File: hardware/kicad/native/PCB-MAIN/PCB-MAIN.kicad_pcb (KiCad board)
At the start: 6 copper layers, 110 x 75 mm, 251 parts, among them J10 U.FL-R-SMT-1(60), J11 USB4105-GF-A-120, J12 MEM2052-00-195-00-A, J13 504050-0291, J6 2336582-1, J7 2336582-1, J8 U.FL-R-SMT-1(60), J9 U.FL-R-SMT-1(60), Q1 MMBT3904,215, Q2 MMBT3904,215, Q3 MMBT3904,215, Q4 Si1016X-T1-GE3, U1 STM32U585VIT6Q, U10 E22-900M22S, U11 MDBT50Q-P1MV2, U13 TS3A27518EPWR, U14 ESDALC6V1-5P6, U15 ESDALC6V1-5P6, U16 SN74AXC8T245PWR, U17 SN74LVC32APWR, U18 SN74AXC1T45DRLR, U19 TPD4E05U06DQAR, U2 W25Q512JVFIQ, U20 TPD4E05U06DQAR, U21 TPD4E05U06DQAR, U22 TPD4E05U06DQAR, U23 TPD4E05U06DQAR, U24 TPD4E05U06DQAR, U25 TPD2EUSB30DRTR, U26 TPD2EUSB30DRTR, U27 TPD4E05U06DQAR, U3 LIS2DW12TR, U4 STTS22HTR, U5 LT6000IDCB#TRMPBF, U6 SN74LVC1G07DBVR, U7 SN74AXC8T245PWR, U8 BG95-M3, U9 MAX-M10S-00B, X1 SiT1552AI-JE-DCC-32.768D

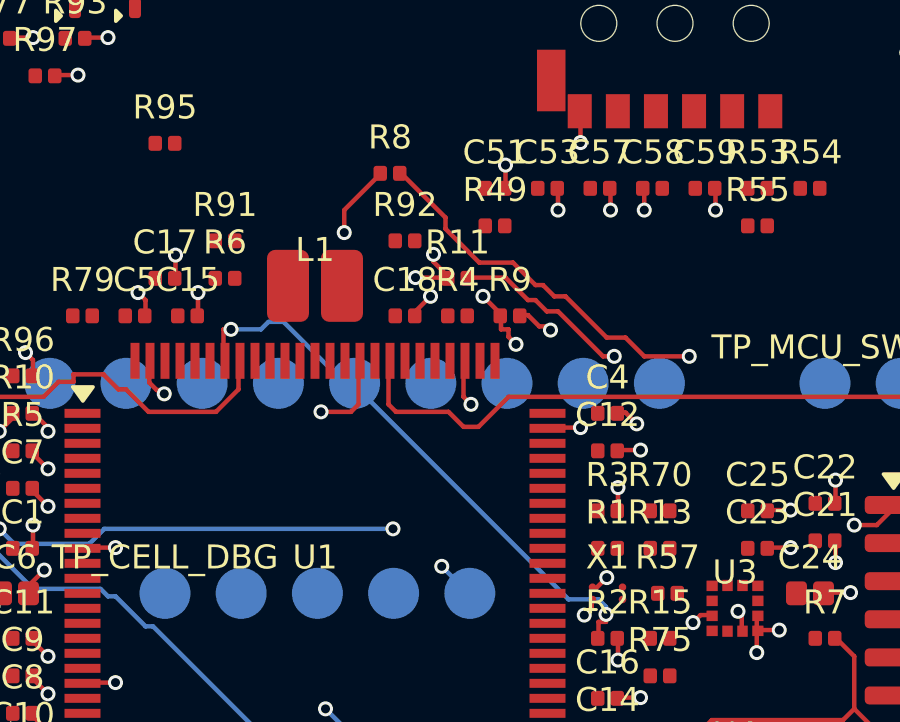
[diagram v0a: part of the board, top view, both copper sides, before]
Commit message: Apply accepted USB termination placement ECO
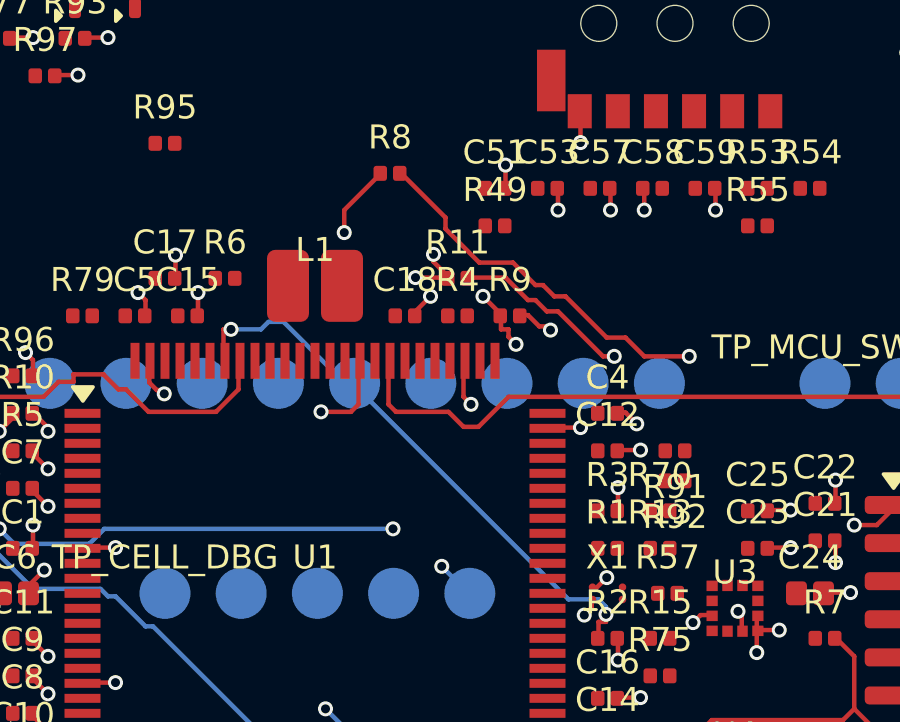
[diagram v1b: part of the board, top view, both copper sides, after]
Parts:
- moved R91 16.6 mm to (64.0, 25.2), turned to 0 degrees
- moved R92 12.0 mm to (64.0, 26.2), turned to 0 degrees
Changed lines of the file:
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@@
   )
   (footprint "" (layer "F.Cu")
-    (at 55 18.25 180)
+    (at 64 26.25)
     (property "DIONEA_COURTYARD_SOURCE" "PCB_MAIN_PASSIVE_COURTYARD_RULE_REV_A")
     (property "DIONEA_COURTYARD_STATUS" "CONTROLLED_PAD_ENVELOPE_PLUS_0.25_MM")
@@
   )
   (footprint "" (layer "F.Cu")
-    (at 49 18.25 180)
-    (property "DIONEA_COURTYARD_SOURCE" "PCB_MAIN_PASSIVE_COURTYARD_RULE_REV_A")
-    (property "DIONEA_COURTYARD_STATUS" "CONTROLLED_PAD_ENVELOPE_PLUS_0.25_MM")
+    (at 64 25.25)
+    (property "DIONEA_COURTYARD_SOURCE" "PCB_MAIN_PASSIVE_COURTYARD_RULE_REV_A")
+    (property "DIONEA_COURTYARD_STATUS" "CONTROLLED_PAD_ENVELOPE_PLUS_0.25_MM")

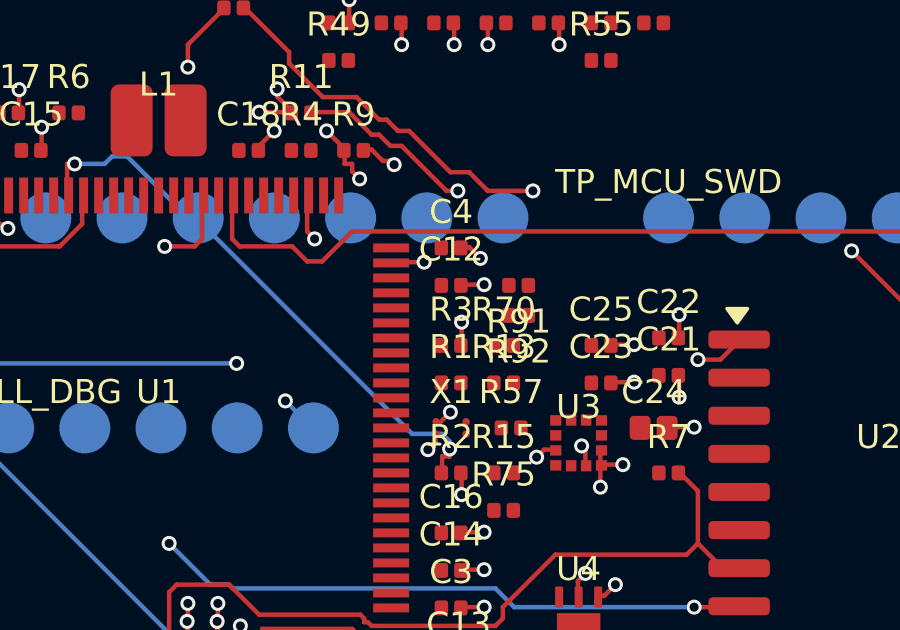
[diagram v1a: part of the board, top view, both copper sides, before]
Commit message: Apply accepted USB MCU source routing
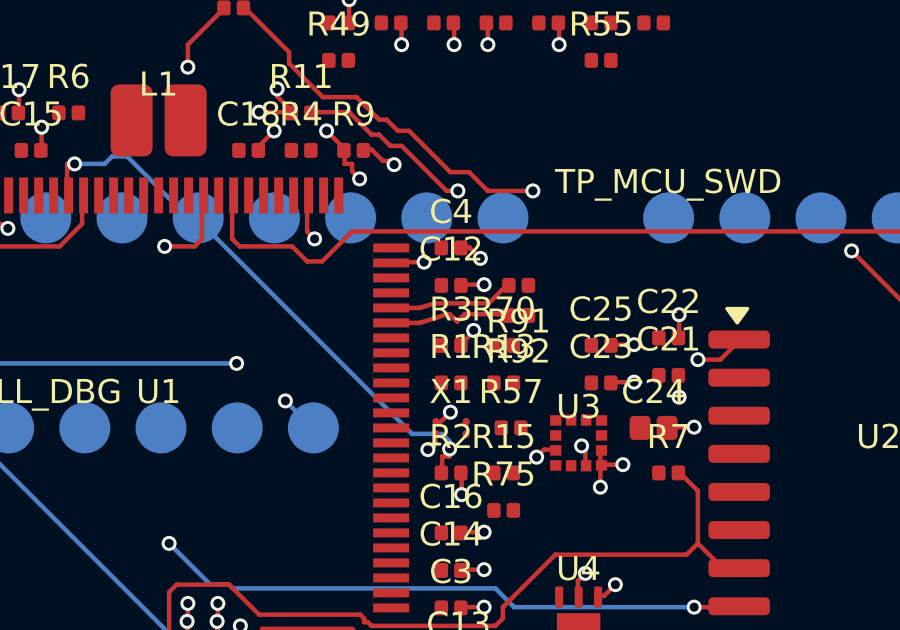
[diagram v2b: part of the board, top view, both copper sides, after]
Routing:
- net USB_DM_U1: track 0.00 -> 4.18 mm
- net USB_DP_U1: track 0.00 -> 4.18 mm
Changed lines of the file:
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@@
   (segment (start 64.849999 30.725) (end 64.599999 30.975) (width 0.15) (layer "F.Cu") (net 45))
   (segment (start 81.475 20.475) (end 81.475 20.1) (width 0.15) (layer "F.Cu") (net 45))
-  (segment (start 62.1 27.225) (end 62.1 26.475) (width 0.15) (layer "F.Cu") (net 45))
+  (segment (start 62.1 27.225) (end 62.5 26.75) (width 0.15) (layer "F.Cu") (net 45))
   (segment (start 65.974999 35.1) (end 66.224999 34.85) (width 0.15) (layer "F.Cu") (net 45))
   (segment (start 46.475 22.225) (end 46.475 22.975) (width 0.15) (layer "F.Cu") (net 45))
@@
   (via (at 103.6 28.475) (size 0.5) (drill 0.3) (layers "F.Cu" "B.Cu") (net 45))
   (via (at 45.85 8.225) (size 0.5) (drill 0.3) (layers "F.Cu" "B.Cu") (net 45))
-  (via (at 62.1 26.475) (size 0.5) (drill 0.3) (layers "F.Cu" "B.Cu") (net 45))
+  (via (at 62.5 26.75) (size 0.5) (drill 0.3) (layers "F.Cu" "B.Cu") (net 45))
   (via (at 67.475 31.225) (size 0.5) (drill 0.3) (layers "F.Cu" "B.Cu") (net 45))
   (via (at 81.475 46.1) (size 0.5) (drill 0.3) (layers "F.Cu" "B.Cu") (net 45))
@@
   (segment (start 57.45 51.95) (end 57.75 52.55) (width 0.15) (layer "F.Cu") (net 45))
   (via (at 57.75 52.55) (size 0.5) (drill 0.3) (layers "F.Cu" "B.Cu") (net 45))
+  (segment (start 59.75 26) (end 60.700000000000003 26) (width 0.1537) (layer "F.Cu") (net 181))
+  (segment (start 60.700000000000003 26) (end 61.200000000000003 25.850000000000001) (width 0.1537) (layer "F.Cu") (net 181))
+  (segment (start 61.200000000000003 25.850000000000001) (end 63 25.850000000000001) (width 0.1537) (layer "F.Cu") (net 181))
+  (segment (start 63 25.850000000000001) (end 63.450000000000003 25.399999999999999) (width 0.1537) (layer "F.Cu") (net 181))
+  (segment (start 63.450000000000003 25.399999999999999) (end 63.674999999999997 25.25) (width 0.1537) (layer "F.Cu") (net 181))
+  (segment (start 59.75 26.5) (end 60.700000000000003 26.5) (width 0.1537) (layer "F.Cu") (net 179))
+  (segment (start 60.700000000000003 26.5) (end 61.200000000000003 26.350000000000001) (width 0.1537) (layer "F.Cu") (net 179))
+  (segment (start 61.200000000000003 26.350000000000001) (end 61.600000000000001 26.206900000000001) (width 0.1537) (layer "F.Cu") (net 179))
+  (segment (start 61.600000000000001 26.206900000000001) (end 61.700000000000003 26.206900000000001) (width 0.1537) (layer "F.Cu") (net 179))
+  (segment (start 61.700000000000003 26.206900000000001) (end 61.950000000000003 26.454798070497958) (width 0.1537) (layer "F.Cu") (net 179))
+  (segment (start 61.950000000000003 26.454798070497958) (end 62.200000000000003 26.206900000000001) (width 0.1537) (layer "F.Cu") (net 179))
+  (segment (start 62.200000000000003 26.206900000000001) (end 63.350000000000001 26.206900000000001) (width 0.1537) (layer "F.Cu") (net 179))
+  (segment (start 63.350000000000001 26.206900000000001) (end 63.674999999999997 26.25) (width 0.1537) (layer "F.Cu") (net 179))
   (zone (net 0) (net_name "") (layers "F.Cu" "In1.Cu" "In2.Cu" "In3.Cu" "In4.Cu" "B.Cu") (name "PCB_MAIN_H1_NO_COPPER_D8_AUTHORITY") (hatch edge 0.5)
     (connect_pads (clearance 0))

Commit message: Apply accepted cellular USB modem routing
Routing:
- net CELL_USB_DM_U8: track 0.00 -> 4.77 mm
- net CELL_USB_DP_U8: track 0.00 -> 4.77 mm
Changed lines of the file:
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@@
   (segment (start 62.200000000000003 26.206900000000001) (end 63.350000000000001 26.206900000000001) (width 0.1537) (layer "F.Cu") (net 179))
   (segment (start 63.350000000000001 26.206900000000001) (end 63.674999999999997 26.25) (width 0.1537) (layer "F.Cu") (net 179))
+  (segment (start 14.85 51.100000000000001) (end 14.15 51.324286504055095) (width 0.1537) (layer "F.Cu") (net 36))
+  (segment (start 14.15 51.324286504055095) (end 11.025 51.324286504055095) (width 0.1537) (layer "F.Cu") (net 36))
+  (segment (start 11.025 51.324286504055095) (end 10.324999999999999 50.75) (width 0.1537) (layer "F.Cu") (net 36))
+  (segment (start 14.85 52.200000000000003) (end 14.15 51.681186504055091) (width 0.1537) (layer "F.Cu") (net 34))
+  (segment (start 14.15 51.681186504055091) (end 11.025 51.681186504055091) (width 0.1537) (layer "F.Cu") (net 34))
+  (segment (start 11.025 51.681186504055091) (end 10.324999999999999 52) (width 0.1537) (layer "F.Cu") (net 34))
   (zone (net 0) (net_name "") (layers "F.Cu" "In1.Cu" "In2.Cu" "In3.Cu" "In4.Cu" "B.Cu") (name "PCB_MAIN_H1_NO_COPPER_D8_AUTHORITY") (hatch edge 0.5)
     (connect_pads (clearance 0))

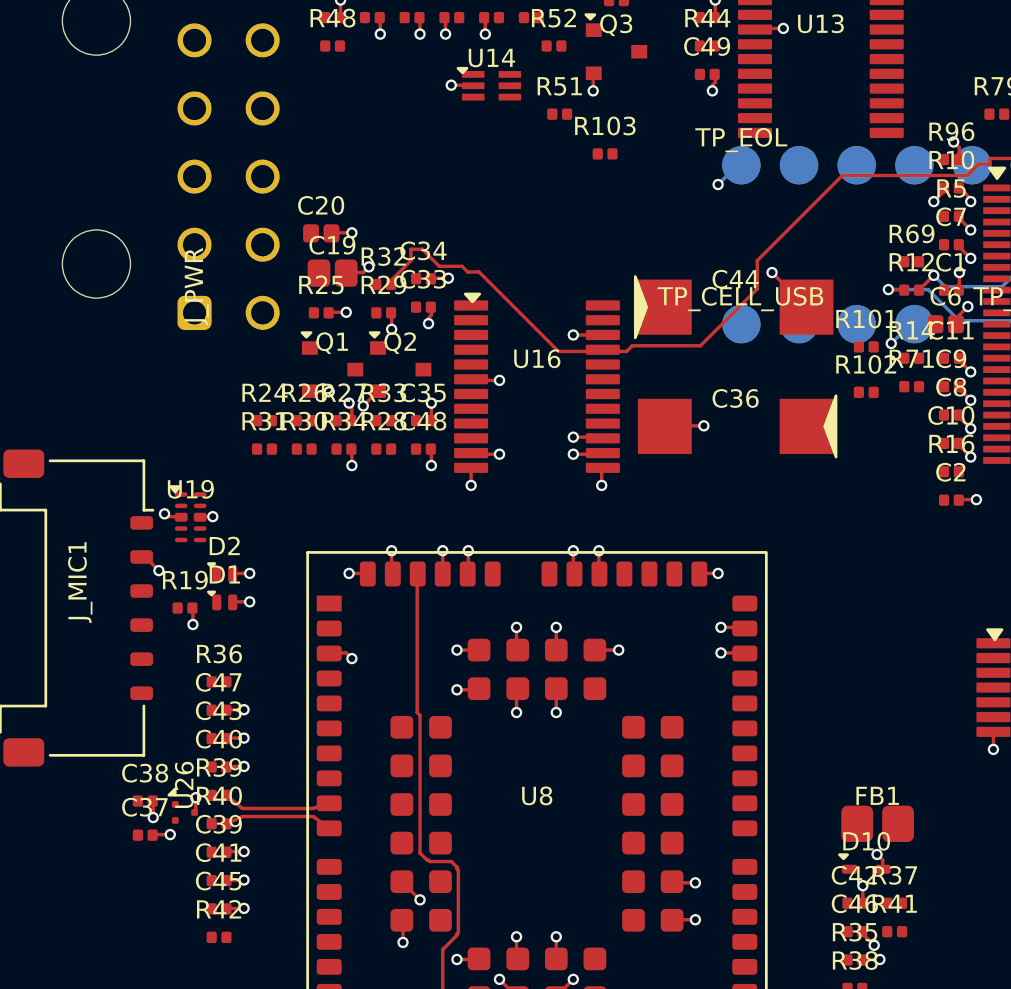
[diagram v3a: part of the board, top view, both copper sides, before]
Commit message: Apply accepted cellular USB fixture routing
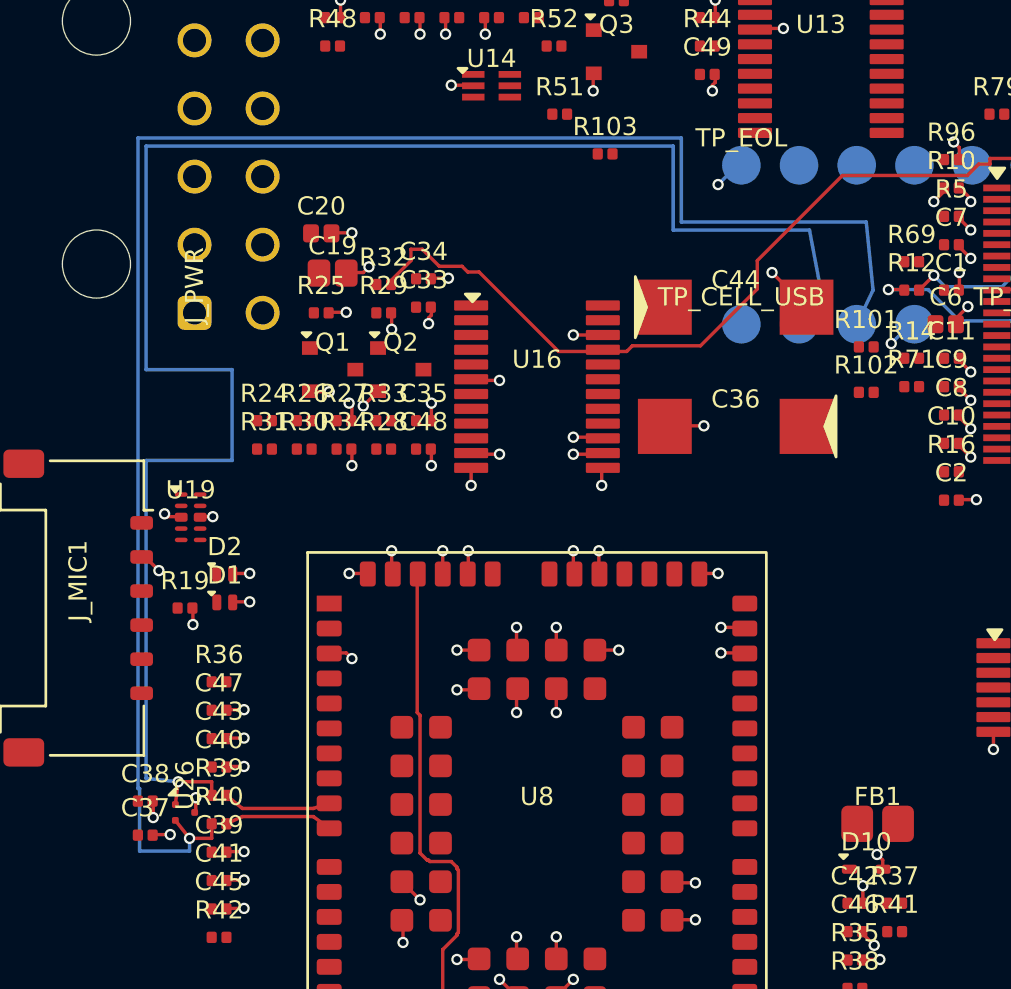
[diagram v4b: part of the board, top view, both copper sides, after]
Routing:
- net CELL_USB_DM_TP: track 0.00 -> 77.3 mm, vias 0 -> 1
- net CELL_USB_DP_TP: track 0.00 -> 77.3 mm, vias 0 -> 1
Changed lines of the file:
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@@
   (segment (start 14.15 51.681186504055091) (end 11.025 51.681186504055091) (width 0.1537) (layer "F.Cu") (net 34))
   (segment (start 11.025 51.681186504055091) (end 10.324999999999999 52) (width 0.1537) (layer "F.Cu") (net 34))
+  (segment (start 9.675000000000001 50.75) (end 9.675000000000001 50.149999999999999) (width 0.1537) (layer "F.Cu") (net 35))
+  (segment (start 9.675000000000001 50.149999999999999) (end 8.199999999999999 50.149999999999999) (width 0.1537) (layer "F.Cu") (net 35))
+  (segment (start 8.199999999999999 50.149999999999999) (end 8.074999999999999 51.149999999999999) (width 0.1537) (layer "F.Cu") (net 35))
+  (segment (start 9.675000000000001 52) (end 9.675000000000001 52.640569415042094) (width 0.1537) (layer "F.Cu") (net 33))
+  (segment (start 9.675000000000001 52.640569415042094) (end 8.699999999999999 52.640569415042094) (width 0.1537) (layer "F.Cu") (net 33))
+  (segment (start 8.699999999999999 52.640569415042094) (end 8.074999999999999 51.850000000000001) (width 0.1537) (layer "F.Cu") (net 33))
+  (segment (start 8.199999999999999 50.149999999999999) (end 6.7869 50) (width 0.1537) (layer "B.Cu") (net 35))
+  (segment (start 6.7869 50) (end 6.7869 36) (width 0.1537) (layer "B.Cu") (net 35))
+  (segment (start 6.7869 36) (end 10.572249357621711 36) (width 0.1537) (layer "B.Cu") (net 35))
+  (segment (start 10.572249357621711 36) (end 10.572249357621711 32) (width 0.1537) (layer "B.Cu") (net 35))
+  (segment (start 10.572249357621711 32) (end 6.7869 32) (width 0.1537) (layer "B.Cu") (net 35))
+  (segment (start 6.7869 32) (end 6.7869 22.1569) (width 0.1537) (layer "B.Cu") (net 35))
+  (segment (start 6.7869 22.1569) (end 30 22.1569) (width 0.1537) (layer "B.Cu") (net 35))
+  (segment (start 30 22.1569) (end 30 25.8569) (width 0.1537) (layer "B.Cu") (net 35))
+  (segment (start 30 25.8569) (end 36 25.8569) (width 0.1537) (layer "B.Cu") (net 35))
+  (segment (start 36 25.8569) (end 36.5 28.5) (width 0.1537) (layer "B.Cu") (net 35))
+  (segment (start 36.5 28.5) (end 35.539999000000002 30) (width 0.1537) (layer "B.Cu") (net 35))
+  (segment (start 8.699999999999999 52.640569415042094) (end 8.699999999999999 53.200000000000003) (width 0.1537) (layer "B.Cu") (net 33))
+  (segment (start 8.699999999999999 53.200000000000003) (end 6.5 53.200000000000003) (width 0.1537) (layer "B.Cu") (net 33))
+  (segment (start 6.5 53.200000000000003) (end 6.5 50.446125000000002) (width 0.1537) (layer "B.Cu") (net 33))
+  (segment (start 6.5 50.446125000000002) (end 6.43 50.446125000000002) (width 0.1537) (layer "B.Cu") (net 33))
+  (segment (start 6.43 50.446125000000002) (end 6.43 21.800000000000001) (width 0.1537) (layer "B.Cu") (net 33))
+  (segment (start 6.43 21.800000000000001) (end 30.3569 21.800000000000001) (width 0.1537) (layer "B.Cu") (net 33))
+  (segment (start 30.3569 21.800000000000001) (end 30.3569 25.5) (width 0.1537) (layer "B.Cu") (net 33))
+  (segment (start 30.3569 25.5) (end 38.5 25.5) (width 0.1537) (layer "B.Cu") (net 33))
+  (segment (start 38.5 25.5) (end 38.799999999999997 28.5) (width 0.1537) (layer "B.Cu") (net 33))
+  (segment (start 38.799999999999997 28.5) (end 38.079999000000001 30) (width 0.1537) (layer "B.Cu") (net 33))
+  (via (at 8.199999999999999 50.149999999999999) (size 0.5) (drill 0.3) (layers "F.Cu" "B.Cu") (net 35))
+  (via (at 8.699999999999999 52.640569415042094) (size 0.5) (drill 0.3) (layers "F.Cu" "B.Cu") (net 33))
   (zone (net 0) (net_name "") (layers "F.Cu" "In1.Cu" "In2.Cu" "In3.Cu" "In4.Cu" "B.Cu") (name "PCB_MAIN_H1_NO_COPPER_D8_AUTHORITY") (hatch edge 0.5)
     (connect_pads (clearance 0))

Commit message: apply: tools/apply_pcb_main_inner_reroute_003_application_rev_a.py
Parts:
- moved R10 20.2 mm to (62.0, 19.8), turned to 90 degrees
- moved R11 6.75 mm to (63.5, 19.8), turned to 90 degrees
- moved R9 2.24 mm to (60.5, 19.8), turned to 90 degrees
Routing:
- net NOR_IO2_U1: track 40.7 -> 23.6 mm, vias 4 -> 2
- net GND_MODEM: track 88.6 -> 101.3 mm
- net NOR_IO0_U1: track 40.5 -> 30.8 mm, vias 4 -> 2
- net NOR_NCS_U2: track 26.5 -> 24.1 mm, vias 0 -> 2
- net NOR_IO3_U2: track 31.5 -> 33.5 mm, vias 3 -> 2
- net NOR_IO0_U2: track 24.9 -> 23.8 mm
- net EN_MODEM: track 43.5 -> 44.5 mm, vias 1 -> 2
- net NOR_IO1_U2: track 33.8 -> 32.9 mm, vias 3 -> 2
- net NOR_CLK_U1: track 24.9 -> 24.2 mm
- net NOR_IO1_U1: track 22.3 -> 21.7 mm
- net NOR_IO2_U2: track 30.5 -> 31.0 mm
- net SD_D2_U1: track 35.9 -> 35.7 mm, vias 2 -> 0
- net GND_DIGITAL: vias 136 -> 160
- added copper zone on In4.Cu, net GND_DIGITAL
